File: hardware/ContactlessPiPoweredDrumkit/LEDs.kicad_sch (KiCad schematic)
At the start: 6 parts

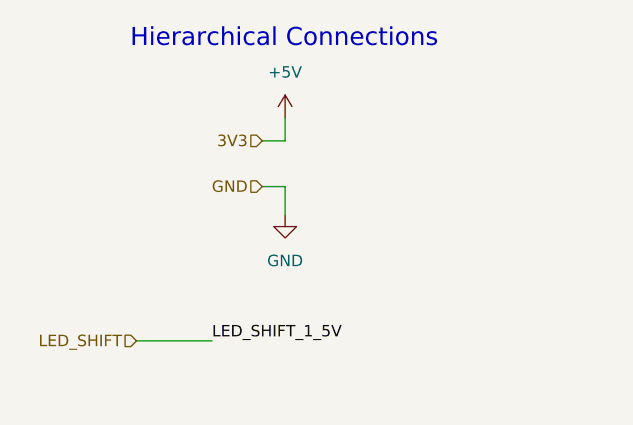
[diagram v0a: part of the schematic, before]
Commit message: Add Hierarchical Connections and Distance Sensors
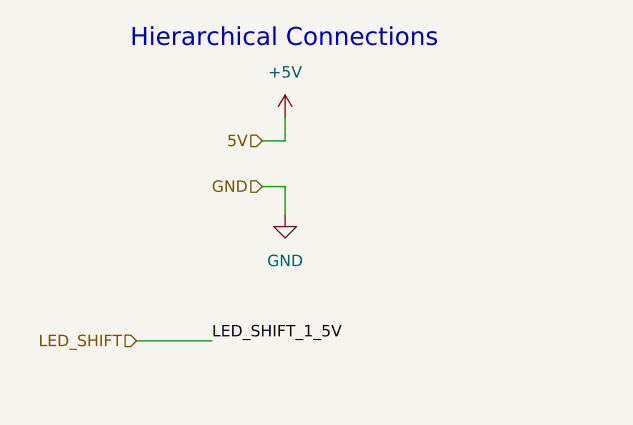
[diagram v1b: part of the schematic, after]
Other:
- title: (none) -> LEDs
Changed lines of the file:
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@@
 (kicad_sch (version 20230121) (generator eeschema)
   (paper "A4")
+  (title_block
+    (title "LEDs")
+    (rev "A")
+  )
   (wire (pts (xy 151.003 34.798) (xy 151.003 39.37))
     (stroke (width 0) (type default))
@@
     (effects (font (size 1.27 1.27)) (justify right))
   )
-  (hierarchical_label "3V3" (shape input) (at 42.545 31.75 180) (fields_autoplaced)
+  (hierarchical_label "5V" (shape input) (at 42.545 31.75 180) (fields_autoplaced)
     (effects (font (size 1.27 1.27)) (justify right))
   )

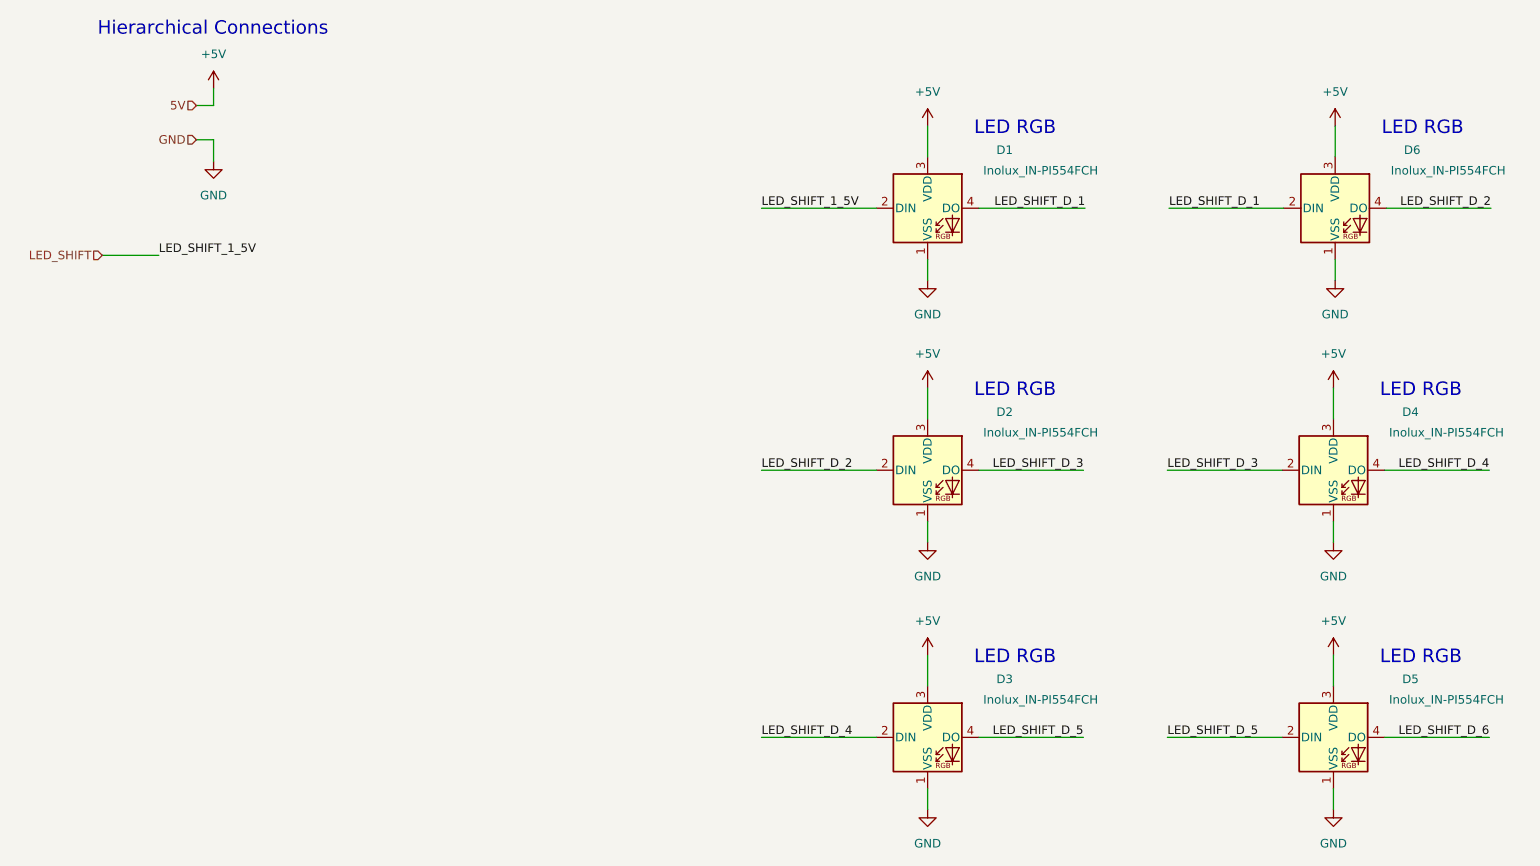
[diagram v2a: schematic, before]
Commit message: Complete PCB Layout
Completed PCB layout
Custom Artwork
Generate Gerbers
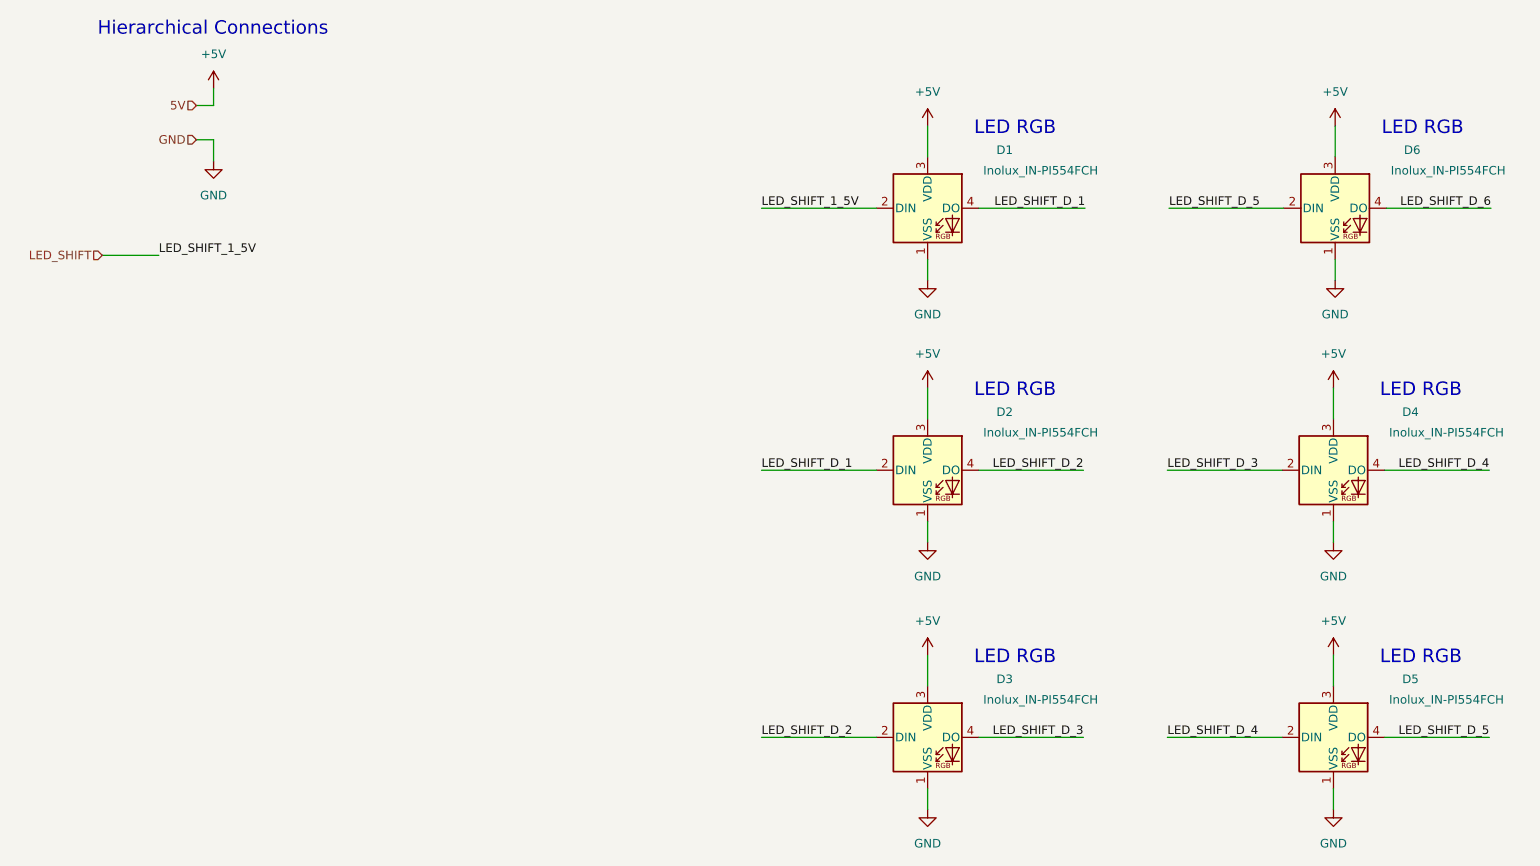
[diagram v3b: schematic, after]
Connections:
- net LED_SHIFT_D_1: now also D2.2 (DIN); no longer D6.2 (DIN)
- net LED_SHIFT_D_2: now also D2.4 (DO), D3.2 (DIN); no longer D2.2 (DIN), D6.4 (DO)
- net LED_SHIFT_D_3: now also D3.4 (DO); no longer D2.4 (DO)
- net LED_SHIFT_D_4: now also D5.2 (DIN); no longer D3.2 (DIN)
- net LED_SHIFT_D_5: now also D5.4 (DO), D6.2 (DIN); no longer D3.4 (DO), D5.2 (DIN)
- net LED_SHIFT_D_6: now also D6.4 (DO); no longer D5.4 (DO)
